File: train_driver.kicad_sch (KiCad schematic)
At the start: 40 parts, among them J1 Screw_Terminal_01x02, J2 Screw_Terminal_01x02, J3 Screw_Terminal_01x02, J4 Screw_Terminal_01x02, J5 Screw_Terminal_01x06, J6 Screw_Terminal_01x02, J7 Screw_Terminal_01x02, J8 Screw_Terminal_01x02, Q2 IRF3205, Q3 IRF3205, U1 YAAJ_BluePill_Part_Like, U2 L7805, U3 YAAJ_DCDC_StepDown_LM2596

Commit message: docs: add schematic name
Signed-off-by: Scott Gibb <smgibb@yahoo.com>
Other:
- title: (none) -> Train Driver 
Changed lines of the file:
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@@
 	(generator_version "10.0")
 	(paper "A4")
+	(title_block
+		(title "Train Driver ")
+		(comment 1 "A simple MCU Circuit for driving two PWM trains")
+	)
 	(rectangle
 		(start 12.7 13.97)

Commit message: feat: Train Driver Duble Inverting Transisters
Added additional transisters to aid with turning the FET fully on and off to reduce the heat dissipation. Thanks to Gemni and ChatGPT for their suggestions and choosing power components.
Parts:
- removed C5, C6: 1000u, symbol Device:C_Polarized
- removed C7, C8: 100n, symbol Device:C
- removed D5, D7: 1N4148, Diode_THT:D_DO-35_SOD27_P7.62mm_Horizontal, symbol Diode:1N4148
- removed D6, D8: 1N5822, Diode_THT:D_DO-201AD_P15.24mm_Horizontal, symbol Diode:1N5822
- removed F1, F2: Fuse, symbol Device:Fuse
- removed HS3, HS4: Heatsink_Pad_2Pin, symbol Mechanical:Heatsink_Pad_2Pin
- removed J2, J3, J4, J6: Screw_Terminal_01x02, symbol Connector:Screw_Terminal_01x02
- removed Q2, Q3: IRF3205, Package_TO_SOT_THT:TO-220-3_Vertical, symbol Transistor_FET:IRF3205
- removed R1, R2: 330, symbol Device:R
- removed R3, R5: 220, symbol Device:R
- removed R4, R6: 10k, symbol Device:R
- added C10, C12: 100n, symbol Device:C
- added C11, C9: 1000u, symbol Device:C_Polarized
- added D10, D12: 1N4007, Diode_THT:D_DO-201AD_P15.24mm_Horizontal, symbol Diode:1N5822
- added D11, D9: 1N4148, Diode_THT:D_DO-35_SOD27_P7.62mm_Horizontal, symbol Diode:1N4148
- added F3, F4: Fuse, symbol Device:Fuse
- added HS6, HS7: Heatsink_Pad_2Pin, symbol Mechanical:Heatsink_Pad_2Pin
- added J10, J11, J12, J9: Screw_Terminal_01x02, symbol Connector:Screw_Terminal_01x02
- added Q1, Q2, Q4, Q6: S8050, Package_TO_SOT_THT:TO-92_Inline, symbol Transistor_BJT:S8050
- added Q5, Q7: IRF3205, Package_TO_SOT_THT:TO-220-3_Vertical, symbol Transistor_FET:IRF3205
- added R10, R17: 1k, symbol Device:R
- added R11, R16, R7, R9: 1K, symbol Device:R
- added R12, R18: 330, symbol Device:R
- added R13, R19: 220, symbol Device:R
- added R14, R15, R20, R21, R22, R8: 10k, symbol Device:R
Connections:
- net +12V: now also C10.1, C11.1, C12.1, C9.1, D10.1 (K), D12.1 (K), F3.1, F4.1, R10.2, R15.2, R17.2, R8.2
- net GND: now also C10.2, C11.2, C12.2, C9.2, J11.2 (Pin_2), J9.2 (Pin_2), Q1.1 (E), Q2.1 (E), Q4.1 (E), Q5.3 (S), Q6.1 (E), Q7.3 (S), R14.1, R20.1, R21.1, R22.1
- net chl_0_led: now also R12.1, R18.1
- new net: Q2.3 (C), R15.1, R16.1
- new net: Q2.2 (B), R11.2, R22.2
- new net: D11.2 (A), Q7.1 (G), R19.1, R20.2
- new net: F3.2, J10.1 (Pin_1)
- new net: D10.2 (A), J10.2 (Pin_2), Q5.2 (D)
- new net: Q1.2 (B), R21.2, R7.2
- new net: Q1.3 (C), R8.1, R9.1
- new net: F4.2, J12.1 (Pin_1)
- new net: D12.2 (A), J12.2 (Pin_2), Q7.2 (D)
- new net: D11.1 (K), Q6.3 (C), R17.1, R19.2
- new net: J11.1 (Pin_1), R18.2
- new net: D9.2 (A), Q5.1 (G), R13.1, R14.2
- new net: D9.1 (K), Q4.3 (C), R10.1, R13.2
- new net: J9.1 (Pin_1), R12.2
- new net: Q4.2 (B), R9.2
- new net: Q6.2 (B), R16.2
- new net ch_0_pwm: R11.1, R7.1
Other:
- note removed: "FET Driver"
- moved on the sheet: C1, C2, C3, C4, D1, D2, D3, D4, J1, J5, J7, J8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

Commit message: feat: removing led pwm circuitry
Just going to have it driven directly off the 12V circuit.Deliberatly
unfused so that you can see when the fuse is blown

Signed-off-by: Scott Gibb <smgibb@yahoo.com>
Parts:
- R12, R18: value 330 -> 1K
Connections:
- net +12V: now also R12.1, R18.1
- net GND: no longer J11.2 (Pin_2), J9.2 (Pin_2)
- net at D10.2 (A), J10.2 (Pin_2), Q5.2 (D): now also J9.2 (Pin_2)
- net at D12.2 (A), J12.2 (Pin_2), Q7.2 (D): now also J11.2 (Pin_2)
- removed net chl_0_led: R12.1, R18.1, U1.31 (PA6)
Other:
- note added: "LED"
- moved on the sheet: C10, C11, C12, C9, D11, D12, F4, HS7, J11, J12, J9, Q2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

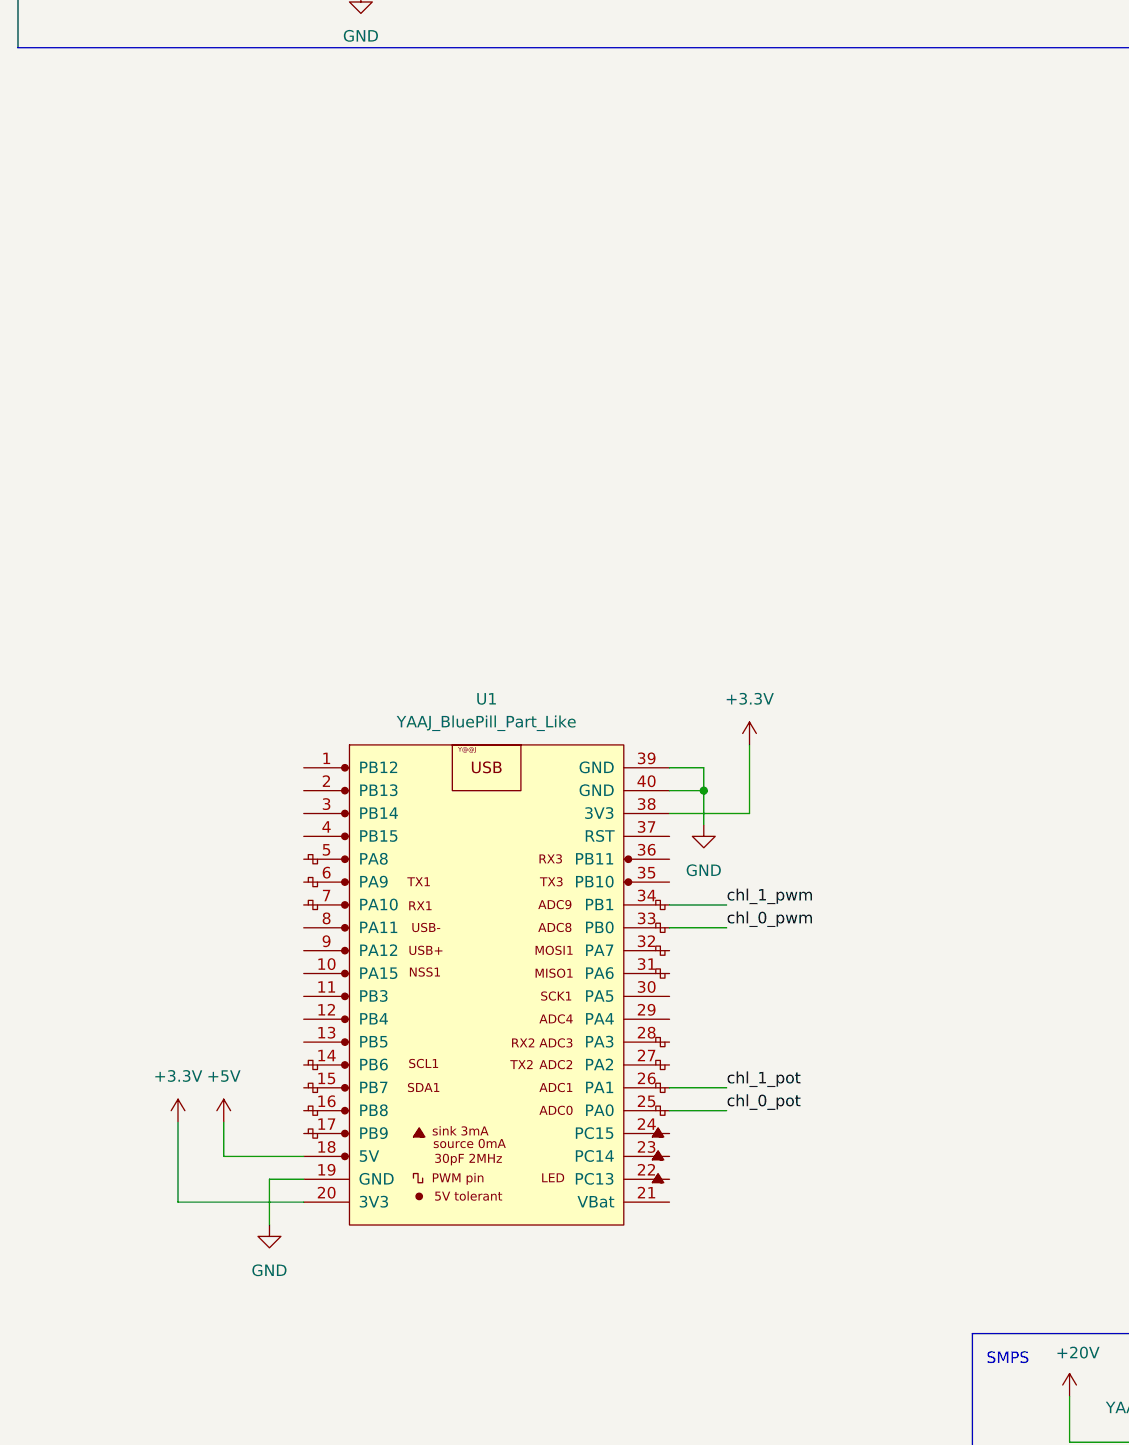
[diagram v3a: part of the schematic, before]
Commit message: feat: add .gitignore and remove .history
Signed-off-by: Scott Gibb <smgibb@yahoo.com>
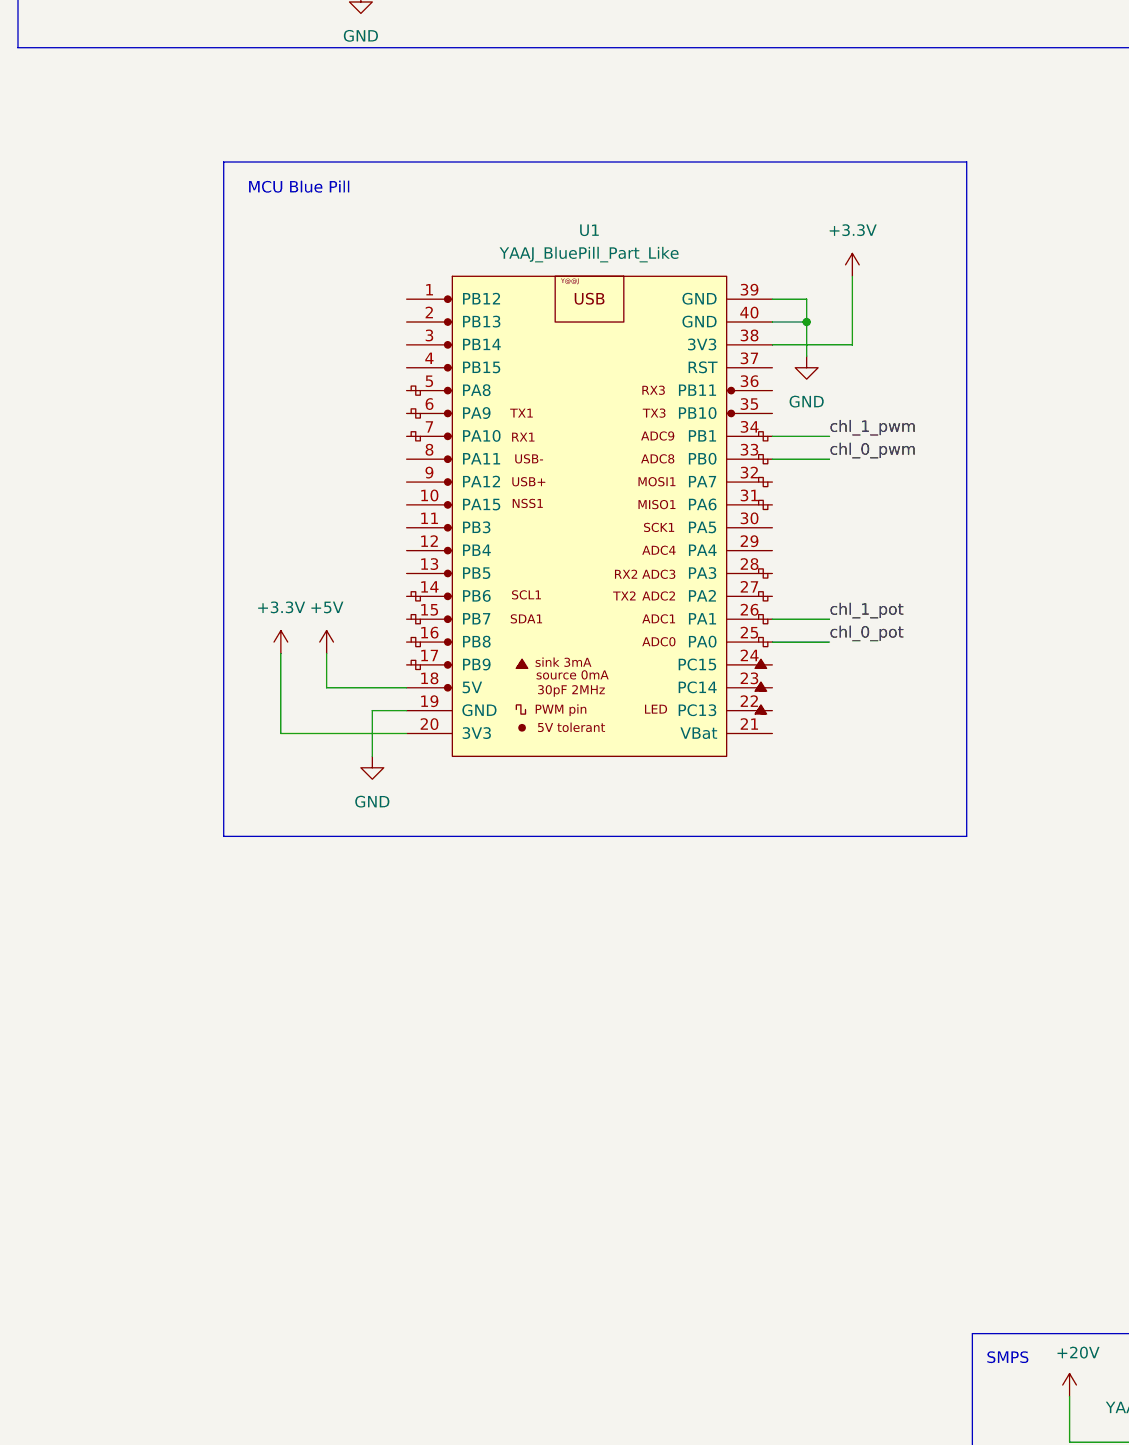
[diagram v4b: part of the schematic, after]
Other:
- note added: "MCU Blue Pill"
- moved on the sheet: U1
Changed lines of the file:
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@@
 	)
 	(rectangle
+		(start 36.83 113.03)
+		(end 119.38 187.96)
+		(stroke
+			(width 0)
+			(type default)
+		)
+		(fill
+			(type none)
+		)
+	)
+	(rectangle
 		(start 184.15 245.11)
 		(end 266.7 276.86)
@@
 		)
 	)
+	(text "MCU Blue Pill\n"
+		(exclude_from_sim no)
+		(at 45.212 116.078 0)
+		(effects
+			(font
+				(size 1.27 1.27)
+			)
+		)
+	)
 	(junction
 		(at 257.81 262.89)
@@
 	)
 	(junction
-		(at 90.17 182.88)
+		(at 101.6 130.81)
 		(diameter 0)
 		(color 0 0 0 0)
@@
 	(wire
 		(pts
-			(xy 36.83 219.71) (xy 36.83 223.52)
+			(xy 48.26 167.64) (xy 48.26 171.45)
 		)
 		(stroke
@@
 	(wire
 		(pts
-			(xy 86.36 218.44) (xy 92.71 218.44)
+			(xy 97.79 166.37) (xy 104.14 166.37)
 		)
 		(stroke
@@
 	(wire
 		(pts
-			(xy 86.36 195.58) (xy 92.71 195.58)
+			(xy 97.79 143.51) (xy 104.14 143.51)
 		)
 		(stroke
@@
 	(wire
 		(pts
-			(xy 95.25 177.8) (xy 95.25 185.42)
+			(xy 106.68 125.73) (xy 106.68 133.35)
 		)
 		(stroke
@@
 	(wire
 		(pts
-			(xy 86.36 185.42) (xy 95.25 185.42)
+			(xy 97.79 133.35) (xy 106.68 133.35)
 		)
 		(stroke
@@
 	(wire
 		(pts
-			(xy 86.36 182.88) (xy 90.17 182.88)
+			(xy 97.79 130.81) (xy 101.6 130.81)
 		)
 		(stroke
@@
 	(wire
 		(pts
-			(xy 90.17 182.88) (xy 90.17 180.34)
+			(xy 101.6 130.81) (xy 101.6 128.27)
 		)
 		(stroke
@@
 	(wire
 		(pts
-			(xy 90.17 180.34) (xy 86.36 180.34)
+			(xy 101.6 128.27) (xy 97.79 128.27)
 		)
 		(stroke
@@
 	(wire
 		(pts
-			(xy 86.36 198.12) (xy 92.71 198.12)
+			(xy 97.79 146.05) (xy 104.14 146.05)
 		)
 		(stroke
@@
 	(wire
 		(pts
-			(xy 31.75 219.71) (xy 31.75 228.6)
+			(xy 43.18 167.64) (xy 43.18 176.53)
 		)
 		(stroke
@@
 	(wire
 		(pts
-			(xy 86.36 215.9) (xy 92.71 215.9)
+			(xy 97.79 163.83) (xy 104.14 163.83)
 		)
 		(stroke
@@
 	(wire
 		(pts
-			(xy 41.91 231.14) (xy 41.91 226.06)
+			(xy 53.34 179.07) (xy 53.34 173.99)
 		)
 		(stroke
@@
 	(wire
 		(pts
-			(xy 41.91 226.06) (xy 45.72 226.06)
+			(xy 53.34 173.99) (xy 57.15 173.99)
 		)
 		(stroke
@@
 	(wire
 		(pts
-			(xy 45.72 228.6) (xy 31.75 228.6)
+			(xy 57.15 176.53) (xy 43.18 176.53)
 		)
 		(stroke
@@
 	(wire
 		(pts
-			(xy 90.17 182.88) (xy 90.17 186.69)
+			(xy 101.6 130.81) (xy 101.6 134.62)
 		)
 		(stroke
@@
 	(wire
 		(pts
-			(xy 36.83 223.52) (xy 45.72 223.52)
+			(xy 48.26 171.45) (xy 57.15 171.45)
 		)
 		(stroke
@@
 	)
 	(label ""
-		(at 86.36 200.66 0)
+		(at 97.79 148.59 0)
 		(effects
 			(font
@@
 	)
 	(label "chl_0_pot"
-		(at 92.71 218.44 0)
+		(at 104.14 166.37 0)
 		(effects
 			(font
@@
 	)
 	(label "chl_1_pot"
-		(at 92.71 215.9 0)
+		(at 104.14 163.83 0)
 		(effects
 			(font
@@
 	)
 	(label "chl_1_pwm"
-		(at 92.71 195.58 0)
+		(at 104.14 143.51 0)
 		(effects
 			(font
@@
 	)
 	(label ""
-		(at 86.36 215.9 0)
+		(at 97.79 163.83 0)
 		(effects
 			(font
@@
 	)
 	(label "chl_0_pwm"
-		(at 92.71 198.12 0)
+		(at 104.14 146.05 0)
 		(effects
 			(font
@@
 	(symbol
 		(lib_id "power:+3.3V")
-		(at 31.75 219.71 0)
+		(at 43.18 167.64 0)
 		(unit 1)
 		(body_style 1)
@@
 		(fields_autoplaced yes)
 		(property "Reference" "#PWR05"
-			(at 31.75 223.52 0)
+			(at 43.18 171.45 0)
 			(hide yes)
 			(show_name no)
@@
 		)
 		(property "Value" "+3.3V"
-			(at 31.75 214.63 0)
+			(at 43.18 162.56 0)
 			(show_name no)
 			(do_not_autoplace no)
@@
 		)
 		(property "Footprint" ""
-			(at 31.75 219.71 0)
+			(at 43.18 167.64 0)
 			(hide yes)
 			(show_name no)
@@
 		)
 		(property "Datasheet" ""
-			(at 31.75 219.71 0)
+			(at 43.18 167.64 0)
 			(hide yes)
 			(show_name no)
@@
 		)
 		(property "Description" "Power symbol creates a global label with name \"+3.3V\""
-			(at 31.75 219.71 0)
+			(at 43.18 167.64 0)
 			(hide yes)
 			(show_name no)
@@
 	(symbol
 		(lib_id "power:GND")
-		(at 90.17 186.69 0)
+		(at 101.6 134.62 0)
 		(unit 1)
 		(body_style 1)
@@
 		(fields_autoplaced yes)
 		(property "Reference" "#PWR02"
-			(at 90.17 193.04 0)
+			(at 101.6 140.97 0)
 			(hide yes)
 			(show_name no)
@@
 		)
 		(property "Value" "GND"
-			(at 90.17 191.77 0)
+			(at 101.6 139.7 0)
 			(show_name no)
 			(do_not_autoplace no)
@@
 		)
 		(property "Footprint" ""
-			(at 90.17 186.69 0)
+			(at 101.6 134.62 0)
 			(hide yes)
 			(show_name no)
@@
 		)
 		(property "Datasheet" ""
-			(at 90.17 186.69 0)
+			(at 101.6 134.62 0)
 			(hide yes)
 			(show_name no)
@@
 		)
 		(property "Description" "Power symbol creates a global label with name \"GND\" , ground"
-			(at 90.17 186.69 0)
+			(at 101.6 134.62 0)
 			(hide yes)
 			(show_name no)
@@
 	(symbol
 		(lib_id "power:GND")
-		(at 41.91 231.14 0)
+		(at 53.34 179.07 0)
 		(unit 1)
 		(body_style 1)
@@
 		(fields_autoplaced yes)
 		(property "Reference" "#PWR03"
-			(at 41.91 237.49 0)
+			(at 53.34 185.42 0)
 			(hide yes)
 			(show_name no)
@@
 		)
 		(property "Value" "GND"
-			(at 41.91 236.22 0)
+			(at 53.34 184.15 0)
 			(show_name no)
 			(do_not_autoplace no)
@@
 		)
 		(property "Footprint" ""
-			(at 41.91 231.14 0)
+			(at 53.34 179.07 0)
 			(hide yes)
 			(show_name no)
@@
 		)
 		(property "Datasheet" ""
-			(at 41.91 231.14 0)
+			(at 53.34 179.07 0)
 			(hide yes)
 			(show_name no)
@@
 		)
 		(property "Description" "Power symbol creates a global label with name \"GND\" , ground"
-			(at 41.91 231.14 0)
+			(at 53.34 179.07 0)
 			(hide yes)
 			(show_name no)
@@
 	(symbol
 		(lib_id "power:+5V")
-		(at 36.83 219.71 0)
+		(at 48.26 167.64 0)
 		(unit 1)
 		(body_style 1)
@@
 		(fields_autoplaced yes)
 		(property "Reference" "#PWR06"
-			(at 36.83 223.52 0)
+			(at 48.26 171.45 0)
 			(hide yes)
 			(show_name no)
@@
 		)
 		(property "Value" "+5V"
-			(at 36.83 214.63 0)
+			(at 48.26 162.56 0)
 			(show_name no)
 			(do_not_autoplace no)
@@
 		)
 		(property "Footprint" ""
-			(at 36.83 219.71 0)
+			(at 48.26 167.64 0)
 			(hide yes)
 			(show_name no)
@@
 		)
 		(property "Datasheet" ""
-			(at 36.83 219.71 0)
+			(at 48.26 167.64 0)
 			(hide yes)
 			(show_name no)
@@
 		)
 		(property "Description" "Power symbol creates a global label with name \"+5V\""
-			(at 36.83 219.71 0)
+			(at 48.26 167.64 0)
 			(hide yes)
 			(show_name no)
@@
 	(symbol
 		(lib_id "power:+3.3V")
-		(at 95.25 177.8 0)
+		(at 106.68 125.73 0)
 		(unit 1)
 		(body_style 1)
@@
 		(fields_autoplaced yes)
 		(property "Reference" "#PWR04"
-			(at 95.25 181.61 0)
+			(at 106.68 129.54 0)
 			(hide yes)
 			(show_name no)
@@
 		)
 		(property "Value" "+3.3V"
-			(at 95.25 172.72 0)
+			(at 106.68 120.65 0)
 			(show_name no)
 			(do_not_autoplace no)
@@
 		)
 		(property "Footprint" ""
-			(at 95.25 177.8 0)
+			(at 106.68 125.73 0)
 			(hide yes)
 			(show_name no)
@@
 		)
 		(property "Datasheet" ""
-			(at 95.25 177.8 0)
+			(at 106.68 125.73 0)
 			(hide yes)
 			(show_name no)
@@
 		)
 		(property "Description" "Power symbol creates a global label with name \"+3.3V\""
-			(at 95.25 177.8 0)
+			(at 106.68 125.73 0)
 			(hide yes)
 			(show_name no)
@@
 	(symbol
 		(lib_id "YAAJ_BluePill_Part_Like:YAAJ_BluePill_Part_Like")
-		(at 66.04 203.2 0)
+		(at 77.47 151.13 0)
 		(unit 1)
 		(body_style 1)
@@
 		(fields_autoplaced yes)
 		(property "Reference" "U1"
-			(at 66.04 172.72 0)
+			(at 77.47 120.65 0)
 			(show_name no)
 			(do_not_autoplace no)
@@
 		)
 		(property "Value" "YAAJ_BluePill_Part_Like"
-			(at 66.04 175.26 0)
+			(at 77.47 123.19 0)
 			(show_name no)
 			(do_not_autoplace no)
@@
 		)
 		(property "Footprint" ""
-			(at 83.82 228.6 0)
+			(at 95.25 176.53 0)
 			(hide yes)
 			(show_name no)
@@
 		)
 		(property "Datasheet" ""
-			(at 83.82 228.6 0)
+			(at 95.25 176.53 0)
 			(hide yes)
 			(show_name no)
@@
 		)
 		(property "Description" "STM32 Blue Pill ; not KLC compliant"
-			(at 66.04 203.2 0)
+			(at 77.47 151.13 0)
 			(hide yes)
 			(show_name no)

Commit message: fix(erc): Addressed all erc warnings
Signed-off-by: Scott Gibb <smgibb@yahoo.com>
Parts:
- removed D1, D2, D3, D4: 1N5822, Diode_THT:D_DO-201AD_P15.24mm_Horizontal, symbol Diode:1N5822
- removed D10, D12: 1N4007, Diode_THT:D_DO-201AD_P15.24mm_Horizontal, symbol Diode:1N5822
- added D1, D3: 1N4002, Diode_THT:D_DO-41_SOD81_P10.16mm_Horizontal, symbol Diode:1N4002
- added D2: 1N4002, Diode_SMD:Diode_Bridge_Diotec_ABS, symbol Diode_Bridge:ABS8
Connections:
- net chl_0_pwm is gone; now on net ch_0_pwm: U1.33 (PB0)
- net +12V: now also C1.1, C3.1, U2.1 (IN), D1.1 (K), D3.1 (K)
- net +20V: now also D2.1 (+); no longer C1.1, C3.1, U2.1 (IN)
- net AC_+: now also D2.4
- net AC_-: now also D2.3
- net GND: now also D2.2 (-)
- net ch_0_pwm: no longer R11.1
- net at J10.2 (Pin_2), J9.2 (Pin_2), Q5.2 (D): now also D1.2 (A)
- net at J11.2 (Pin_2), J12.2 (Pin_2), Q7.2 (D): now also D3.2 (A)
- net chl_1_pwm renamed ch_1_pwm
- net ch_1_pwm: now also R11.1
- new net chl_0_pot: J5.4 (Pin_4), U1.25 (PA0)
- new net chl_1_pot: J5.2 (Pin_2), U1.26 (PA1)
- now unconnected: U1.32 (PA7)
- no-connect marks 0 -> 36
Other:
- company: (none) -> Gibb
- moved on the sheet: C1, C2, C3, C4, HS6, J1, J7, J8, U1, U2, U3
